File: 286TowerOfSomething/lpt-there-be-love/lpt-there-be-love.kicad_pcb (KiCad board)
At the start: 2 copper layers, 126.5 x 65.9 mm, 10 parts, among them J1 Bus_ISA_8bit, J2 DB25_Receptacle_MountingHoles, SW1 SW_DIP_x07, U1 ST78C36ACJ44, U2 74LS688, Y1 24 MHz

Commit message: Layout of lpt-there-be-love just about done
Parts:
- added C10: 180p, Capacitor_SMD:C_0603_1608Metric_Pad1.08x0.95mm_HandSolder, B.Cu at (175.6, 115.3)
- added C11: 180p, Capacitor_SMD:C_0603_1608Metric_Pad1.08x0.95mm_HandSolder, B.Cu at (175.6, 112.6)
- added C12: 180p, Capacitor_SMD:C_0603_1608Metric_Pad1.08x0.95mm_HandSolder, B.Cu at (175.6, 109.9)
- added C13: 180p, Capacitor_SMD:C_0603_1608Metric_Pad1.08x0.95mm_HandSolder, B.Cu at (175.6, 107.1)
- added C14: 180p, Capacitor_SMD:C_0603_1608Metric_Pad1.08x0.95mm_HandSolder, B.Cu at (175.6, 104.3)
- added C15: 180p, Capacitor_SMD:C_0603_1608Metric_Pad1.08x0.95mm_HandSolder, B.Cu at (175.6, 101.5)
- added C16: 180p, Capacitor_SMD:C_0603_1608Metric_Pad1.08x0.95mm_HandSolder, B.Cu at (175.6, 98.7)
- added C17: 180p, Capacitor_SMD:C_0603_1608Metric_Pad1.08x0.95mm_HandSolder, B.Cu at (175.6, 95.9)
- added C18: 180p, Capacitor_SMD:C_0603_1608Metric_Pad1.08x0.95mm_HandSolder, B.Cu at (175.6, 93.2)
- added C19: 180p, Capacitor_SMD:C_0603_1608Metric_Pad1.08x0.95mm_HandSolder, B.Cu at (175.6, 90.4)
- added C20: 180p, Capacitor_SMD:C_0603_1608Metric_Pad1.08x0.95mm_HandSolder, B.Cu at (184.2, 100.5)
- added C21: 180p, Capacitor_SMD:C_0603_1608Metric_Pad1.08x0.95mm_HandSolder, B.Cu at (184.2, 96.9)
- added C22: 180p, Capacitor_SMD:C_0603_1608Metric_Pad1.08x0.95mm_HandSolder, B.Cu at (184.2, 95.1)
- added C23: 180p, Capacitor_SMD:C_0603_1608Metric_Pad1.08x0.95mm_HandSolder, B.Cu at (175.6, 123.7)
- added C3: 100n, Capacitor_SMD:C_0603_1608Metric_Pad1.08x0.95mm_HandSolder, B.Cu at (89.5, 86.4)
- added C4: 100n, Capacitor_SMD:C_0603_1608Metric_Pad1.08x0.95mm_HandSolder, B.Cu at (111.8, 95.9)
- added C5: 1u, Capacitor_SMD:C_0805_2012Metric_Pad1.18x1.45mm_HandSolder, B.Cu at (111.8, 97.8)
- added C6: 22u, Capacitor_SMD:CP_Elec_5x5.3, F.Cu at (103.5, 83.8)
- added C7: 180p, Capacitor_SMD:C_0603_1608Metric_Pad1.08x0.95mm_HandSolder, B.Cu at (184.2, 91.6)
- added C8: 180p, Capacitor_SMD:C_0603_1608Metric_Pad1.08x0.95mm_HandSolder, B.Cu at (175.6, 120.9)
- added C9: 180p, Capacitor_SMD:C_0603_1608Metric_Pad1.08x0.95mm_HandSolder, B.Cu at (175.6, 118.1)
- added R3: 4.7K, Resistor_SMD:R_0603_1608Metric_Pad0.98x0.95mm_HandSolder, B.Cu at (184.2, 89.8)
- added R4: 4.7K, Resistor_SMD:R_0603_1608Metric_Pad0.98x0.95mm_HandSolder, B.Cu at (184.2, 93.3)
- added R5: 4.7K, Resistor_SMD:R_0603_1608Metric_Pad0.98x0.95mm_HandSolder, B.Cu at (184.2, 98.7)
- added R6: 4.7K, Resistor_SMD:R_0603_1608Metric_Pad0.98x0.95mm_HandSolder, B.Cu at (184.2, 102.2)
- added R7: 4.7K, Resistor_SMD:R_0603_1608Metric_Pad0.98x0.95mm_HandSolder, B.Cu at (175.6, 88.6)
- J2: value DB25_Receptacle_MountingHoles -> DB25F
- R1: moved to B.Cu
- moved U2 94.5 mm to (85.7, 86.4)
- moved Y1 66.8 mm to (139.7, 101.7), turned to -90 degrees
- moved C2 63.6 mm to (143.5, 108.0), turned to -90 degrees
- moved C1 60.8 mm to (143.5, 100.3), turned to 90 degrees
- moved R2 60.2 mm to (143.5, 104.1), turned to 90 degrees
- moved SW1 58.2 mm to (99.7, 90.2)
- moved U1 27.7 mm to (118.1, 96.3), turned to 90 degrees
- moved R1 25.1 mm to (89.5, 101.6)
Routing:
- net +5V: track 0.00 -> 288.8 mm, vias 0 -> 12
- net Net-(U1-BUSY): track 0.00 -> 123.7 mm, vias 0 -> 3
- net Net-(U1-PE): track 0.00 -> 122.9 mm, vias 0 -> 3
- net Net-(U1-SLCT): track 0.00 -> 118.0 mm, vias 0 -> 3
- net Net-(U1-~{ACK}): track 0.00 -> 117.9 mm, vias 0 -> 3
- net Net-(U1-PD7): track 0.00 -> 95.3 mm, vias 0 -> 2
- net Net-(U1-PD5): track 0.00 -> 92.3 mm, vias 0 -> 2
- net Net-(U1-PD6): track 0.00 -> 90.8 mm, vias 0 -> 2
- net Net-(U1-PD3): track 0.00 -> 89.4 mm, vias 0 -> 2
- net Net-(U1-PD4): track 0.00 -> 87.7 mm, vias 0 -> 2
- net Net-(U1-PD1): track 0.00 -> 84.6 mm, vias 0 -> 2
- net Net-(U1-PD2): track 0.00 -> 83.9 mm, vias 0 -> 2
- net /~{LPT_CS}: track 0.00 -> 79.5 mm, vias 0 -> 4
- net Net-(U1-PD0): track 0.00 -> 79.0 mm, vias 0 -> 2
- net /A1: track 0.00 -> 71.5 mm, vias 0 -> 3
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- added copper zone on B.Cu, net GND
- added copper zone on F.Cu, net GND

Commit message: Started on silkscreen for lpt-there-be-love
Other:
- board size 126.5 x 65.9 mm -> 104.6 x 65.9 mm
- board text added: "0x378"
- board text added: "DMA1"
- board text added: "DMA3"
- board text added: "IRQ5"
- board text added: "IRQ7"
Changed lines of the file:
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@@
 		(tags "capacitor handsolder")
 		(property "Reference" "C8"
-			(at 3.175 0 360)
+			(at 3.175 0 0)
 			(layer "B.SilkS")
 			(effects
@@
 		)
 		(property "Value" "180p"
-			(at 0 -1.43 360)
+			(at 0 -1.43 0)
 			(layer "B.Fab")
 			(effects
@@
 		)
 		(fp_text user "${REFERENCE}"
-			(at 0 0 360)
+			(at 0 0 0)
 			(layer "B.Fab")
 			(effects
@@
 		(tags "capacitor handsolder")
 		(property "Reference" "C20"
-			(at 0 4.572 360)
+			(at 0 4.572 0)
 			(layer "B.SilkS")
 			(effects
@@
 		)
 		(property "Value" "180p"
-			(at 0 -1.43 360)
+			(at 0 -1.43 0)
 			(layer "B.Fab")
 			(effects
@@
 		)
 		(fp_text user "${REFERENCE}"
-			(at 0 0 360)
+			(at 0 0 0)
 			(layer "B.Fab")
 			(effects
@@
 		(tags "resistor handsolder")
 		(property "Reference" "R4"
-			(at 0 7.747 360)
+			(at 0 7.747 0)
 			(layer "B.SilkS")
 			(effects
@@
 		)
 		(property "Value" "4.7K"
-			(at 0 -1.43 360)
+			(at 0 -1.43 0)
 			(layer "B.Fab")
 			(effects
@@
 		)
 		(fp_text user "${REFERENCE}"
-			(at 0 0 360)
+			(at 0 0 0)
 			(layer "B.Fab")
 			(effects
@@
 		(tags "resistor handsolder")
 		(property "Reference" "R7"
-			(at -3.175 0 360)
+			(at -3.175 0 0)
 			(layer "B.SilkS")
 			(effects
@@
 		)
 		(property "Value" "4.7K"
-			(at 0 -1.43 360)
+			(at 0 -1.43 0)
 			(layer "B.Fab")
 			(effects
@@
 		)
 		(fp_text user "${REFERENCE}"
-			(at 0 0 360)
+			(at 0 0 0)
 			(layer "B.Fab")
 			(effects
@@
 		(tags "capacitor handsolder")
 		(property "Reference" "C21"
-			(at 0 -8.763 360)
+			(at 0 -8.763 0)
 			(layer "B.SilkS")
 			(effects
@@
 		)
 		(property "Value" "180p"
-			(at 0 -1.43 360)
+			(at 0 -1.43 0)
 			(layer "B.Fab")
 			(effects
@@
 		)
 		(fp_text user "${REFERENCE}"
-			(at 0 0 360)
+			(at 0 0 0)
 			(layer "B.Fab")
 			(effects
@@
 		(tags "capacitor handsolder")
 		(property "Reference" "C22"
-			(at 0 -8.255 360)
+			(at 0 -8.255 0)
 			(layer "B.SilkS")
 			(effects
@@
 		)
 		(property "Value" "180p"
-			(at 0 -1.43 360)
+			(at 0 -1.43 0)
 			(layer "B.Fab")
 			(effects
@@
 		)
 		(fp_text user "${REFERENCE}"
-			(at 0 0 360)
+			(at 0 0 0)
 			(layer "B.Fab")
 			(effects
@@
 		(tags "capacitor handsolder")
 		(property "Reference" "C23"
-			(at 3.175 0 360)
+			(at 3.175 0 0)
 			(layer "B.SilkS")
 			(effects
@@
 		)
 		(property "Value" "180p"
-			(at 0 -1.43 360)
+			(at 0 -1.43 0)
 			(layer "B.Fab")
 			(effects
@@
 		)
 		(fp_text user "${REFERENCE}"
-			(at 0 0 360)
+			(at 0 0 0)
 			(layer "B.Fab")
 			(effects
@@
 		(tags "capacitor handsolder")
 		(property "Reference" "C7"
-			(at 0 -7.239 360)
+			(at 0 -7.239 0)
 			(layer "B.SilkS")
 			(effects
@@
 		)
 		(property "Value" "180p"
-			(at 0 -1.43 360)
+			(at 0 -1.43 0)
 			(layer "B.Fab")
 			(effects
@@
 		)
 		(fp_text user "${REFERENCE}"
-			(at 0 0 360)
+			(at 0 0 0)
 			(layer "B.Fab")
 			(effects
@@
 	)
 	(gr_line
-		(start 60 127)
-		(end 60 70)
+		(start 81.915 127)
+		(end 81.915 70)
 		(stroke
 			(width 0.05)
@@
 	(gr_line
 		(start 186.47725 70)
-		(end 60 70)
+		(end 81.915 70)
 		(stroke
 			(width 0.05)
@@
 	(gr_line
 		(start 83.82 127)
-		(end 60 127)
+		(end 81.915 127)
 		(stroke
 			(width 0.05)
@@
 		(layer "F.Fab")
 	)
+	(gr_text "0x378"
+		(at 98.425 105.41 0)
+		(layer "F.SilkS" knockout)
+		(effects
+			(font
+				(size 0.9 0.9)
+				(thickness 0.1)
+			)
+			(justify right)
+		)
+	)
+	(gr_text "DMA3"
+		(at 98.425 95.25 0)
+		(layer "F.SilkS" knockout)
+		(effects
+			(font
+				(size 1 1)
+				(thickness 0.1)
+			)
+			(justify right)
+		)
+	)
+	(gr_text "DMA3"
+		(at 98.425 100.33 0)
+		(layer "F.SilkS" knockout)
+		(effects
+			(font
+				(size 1 1)
+				(thickness 0.1)
+			)
+			(justify right)
+		)
+	)
+	(gr_text "DMA1"
+		(at 98.425 102.87 0)
+		(layer "F.SilkS" knockout)
+		(effects
+			(font
+				(size 1 1)
+				(thickness 0.1)
+			)
+			(justify right)
+		)
+	)
+	(gr_text "IRQ5"
+		(at 98.425 92.71 0)
+		(layer "F.SilkS" knockout)
+		(effects
+			(font
+				(size 1 1)
+				(thickness 0.1)
+			)
+			(justify right)
+		)
+	)
+	(gr_text "IRQ7"
+		(at 98.425 90.17 0)
+		(layer "F.SilkS" knockout)
+		(effects
+			(font
+				(size 1 1)
+				(thickness 0.1)
+			)
+			(justify right)
+		)
+	)
+	(gr_text "DMA1"
+		(at 98.425 97.79 0)
+		(layer "F.SilkS" knockout)
+		(effects
+			(font
+				(size 1 1)
+				(thickness 0.1)
+			)
+			(justify right)
+		)
+	)
 	(dimension
 		(type aligned)
@@
 		(polygon
 			(pts
-				(xy 186.563 133.985) (xy 186.563 69.977) (xy 59.944 69.977) (xy 59.944 127) (xy 83.693 127) (xy 83.693 128.524)
+				(xy 186.563 133.985) (xy 186.563 69.977) (xy 81.534 69.977) (xy 81.534 127) (xy 83.693 127) (xy 83.693 128.524)
 				(xy 165.227 128.524) (xy 165.227 127.127) (xy 174.371 127.127) (xy 174.371 133.985)
 			)

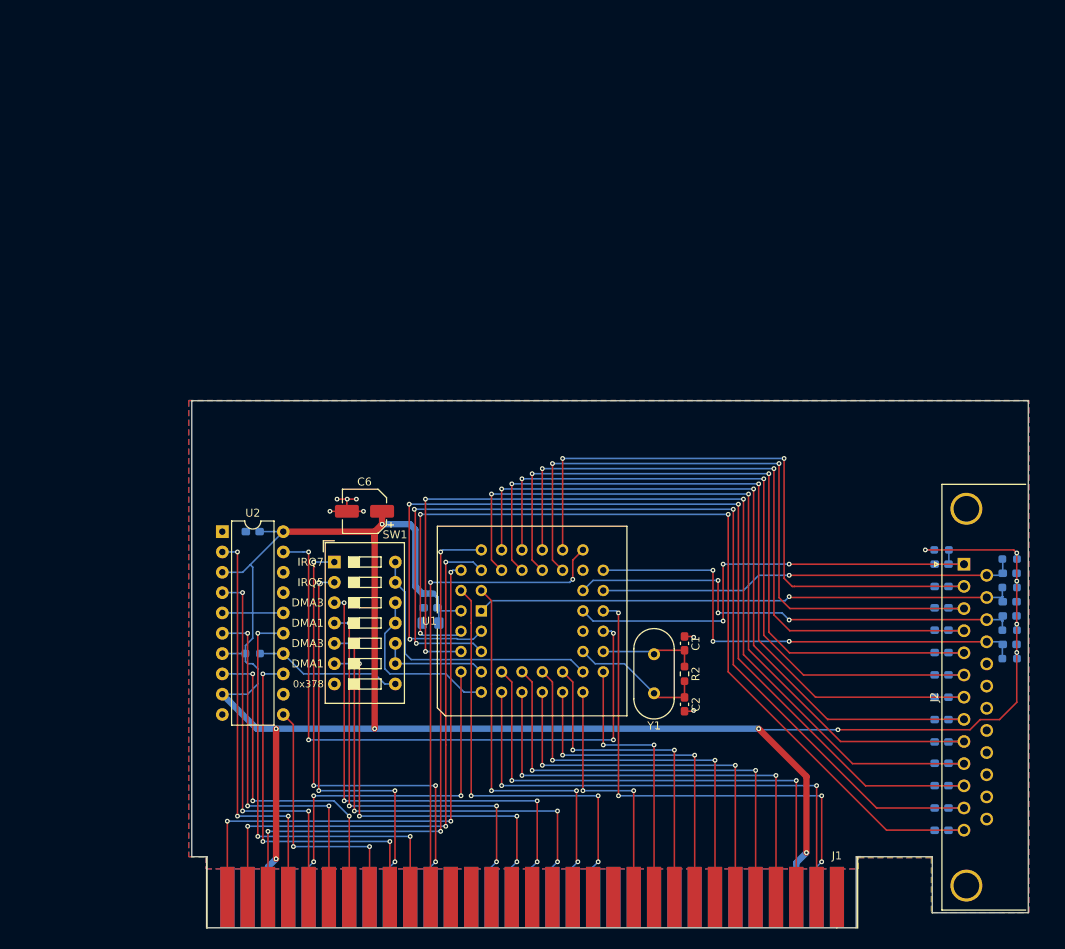
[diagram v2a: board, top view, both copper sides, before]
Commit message: Adding proper bracket to lpt-there-be-love
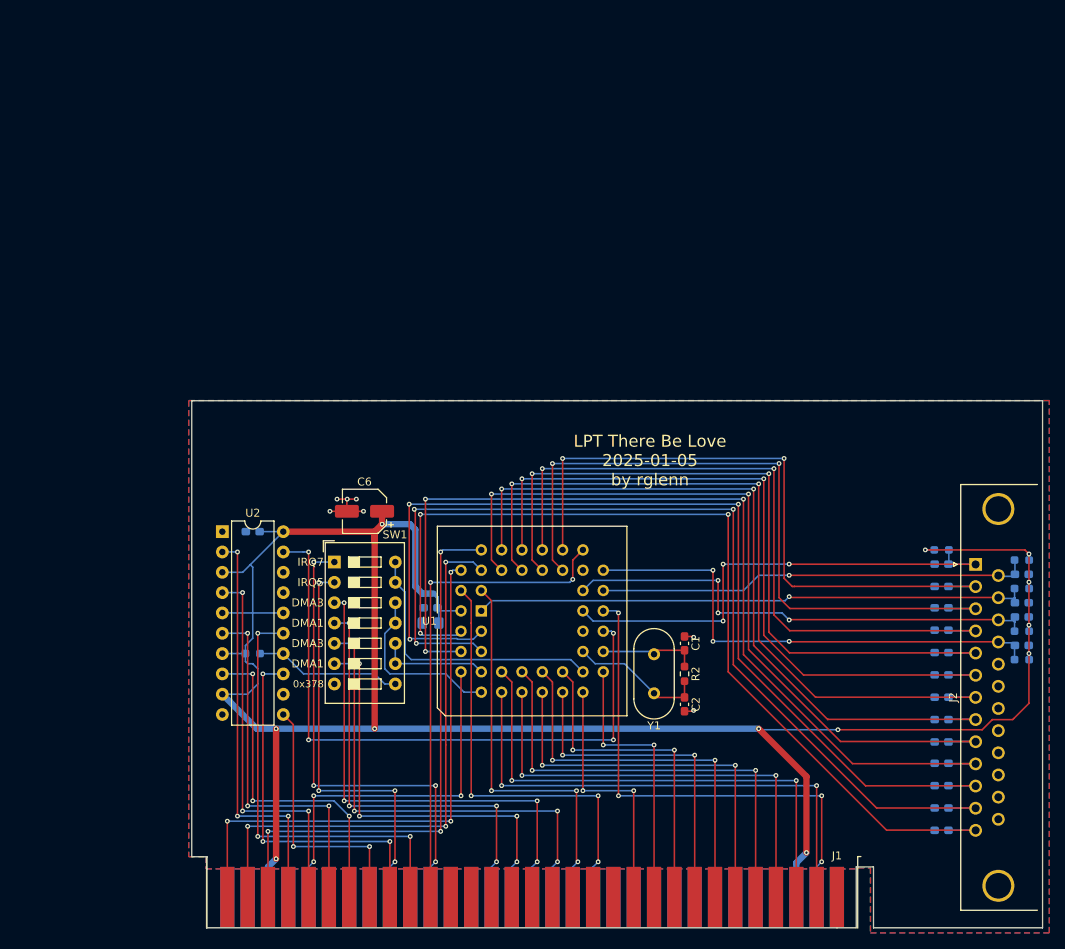
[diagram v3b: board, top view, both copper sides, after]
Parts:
- added BRACKET1: ~, pc-parts:PC_BRACKET_ISA_KEYSTONE_9200_Rev1_1, F.Cu at (162.6, 135.9)
- J2: footprint Connector_Dsub:DSUB-25_Female_Horizontal_P2.77x2.84mm_EdgePinOffset4.94mm_Housed_MountingHolesOffset7.48mm -> Connector_Dsub:DSUB-25_Female_Horizontal_P2.77x2.84mm_EdgePinOffset4.94mm_Housed_MountingHolesOffset4.94mm
- moved C20 1.53 mm to (185.7, 100.6)
- moved C21 1.53 mm to (185.7, 97.0)
- moved C7 1.53 mm to (185.7, 91.7)
- moved C22 1.53 mm to (185.7, 95.2)
- moved R3 1.53 mm to (185.7, 89.9)
- moved R4 1.53 mm to (185.7, 93.5)
- moved R5 1.53 mm to (185.7, 98.8)
- moved R6 1.53 mm to (185.7, 102.4)
- moved J2 1.46 mm to (179.9, 90.5)
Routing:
- net +5V: track 288.8 -> 291.8 mm
- net Net-(U1-PD2): track 83.9 -> 86.9 mm
- net Net-(U1-PD1): track 84.6 -> 87.5 mm
- net Net-(U1-BUSY): track 123.7 -> 126.6 mm
- net Net-(U1-PD6): track 90.8 -> 93.7 mm
- net Net-(U1-PD5): track 92.3 -> 95.2 mm
- net Net-(U1-~{ACK}): track 117.9 -> 120.8 mm
- net Net-(U1-SLCT): track 118.0 -> 121.0 mm
- net Net-(U1-PE): track 122.9 -> 125.9 mm
- net Net-(U1-PD4): track 87.7 -> 90.6 mm
- net Net-(U1-PD3): track 89.4 -> 92.3 mm
- net Net-(U1-PD0): track 79.0 -> 81.9 mm
- net Net-(U1-~{STROBE}): track 59.0 -> 62.0 mm
- net Net-(U1-PD7): track 95.3 -> 98.2 mm
- net Net-(J2-P15): track 67.8 -> 69.2 mm
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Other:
- board size 104.6 x 65.9 mm -> 106.3 x 65.9 mm
- board text added: "LPT There Be Love 2025-01-05 by rglenn"
